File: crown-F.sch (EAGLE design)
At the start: 97 parts

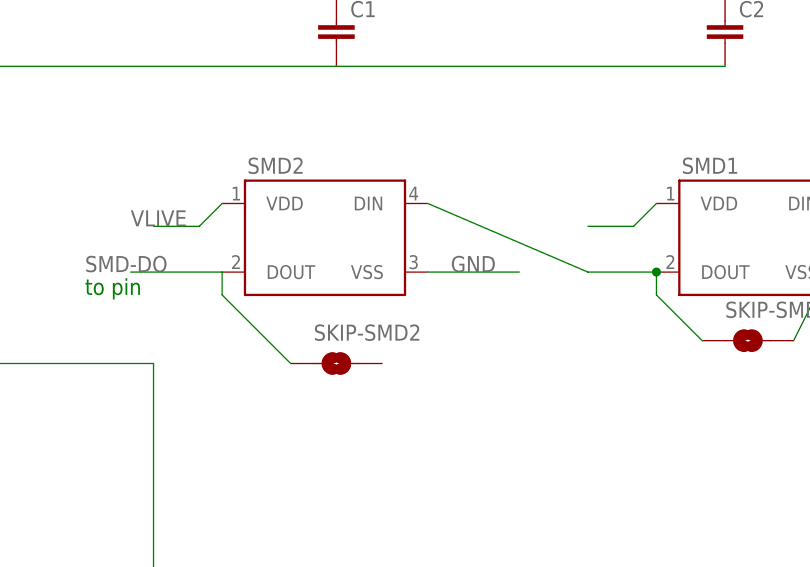
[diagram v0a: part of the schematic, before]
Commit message: forgot a connection on skip-smd bits
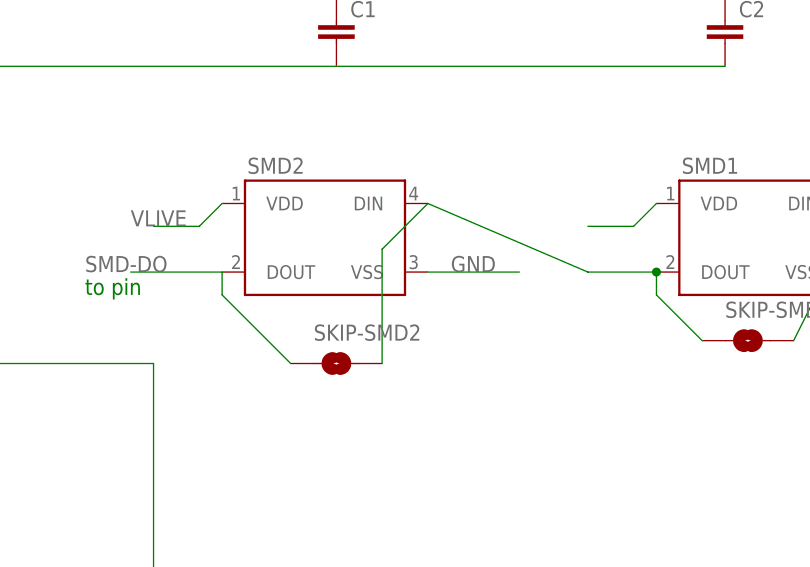
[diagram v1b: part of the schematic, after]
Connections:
- net N$10: now also SKIP-SMD2.2
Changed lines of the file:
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@@
 <pinref part="SMD2" gate="G$1" pin="DIN"/>
 <wire x1="220.98" y1="119.38" x2="203.2" y2="127" width="0.2032" layer="91"/>
+<pinref part="SKIP-SMD2" gate="1" pin="2"/>
+<wire x1="198.12" y1="109.22" x2="198.12" y2="121.92" width="0.2032" layer="91"/>
+<wire x1="198.12" y1="121.92" x2="203.2" y2="127" width="0.2032" layer="91"/>
 </segment>
 </net>
